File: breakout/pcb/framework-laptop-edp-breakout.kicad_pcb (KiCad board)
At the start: 4 copper layers, 46 x 59 mm, 7 parts, among them J1 20879-040E-01, J2 Conn_01x40, J3 Conn_01x01

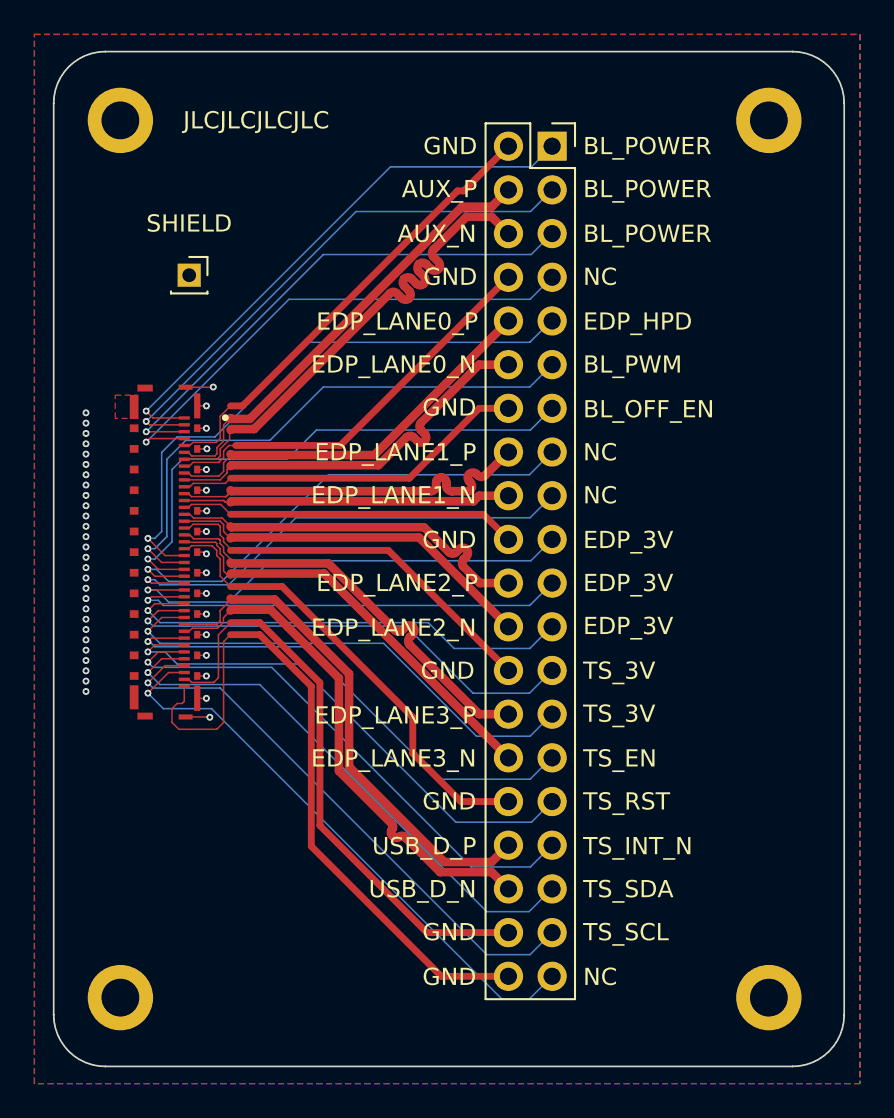
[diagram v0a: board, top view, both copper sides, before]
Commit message: rework breakout because pins were wrong
turns out pin out documentation from framework is reversed - pin 40  in pinouts.md is pin 1 on the data sheet for the ipex connector
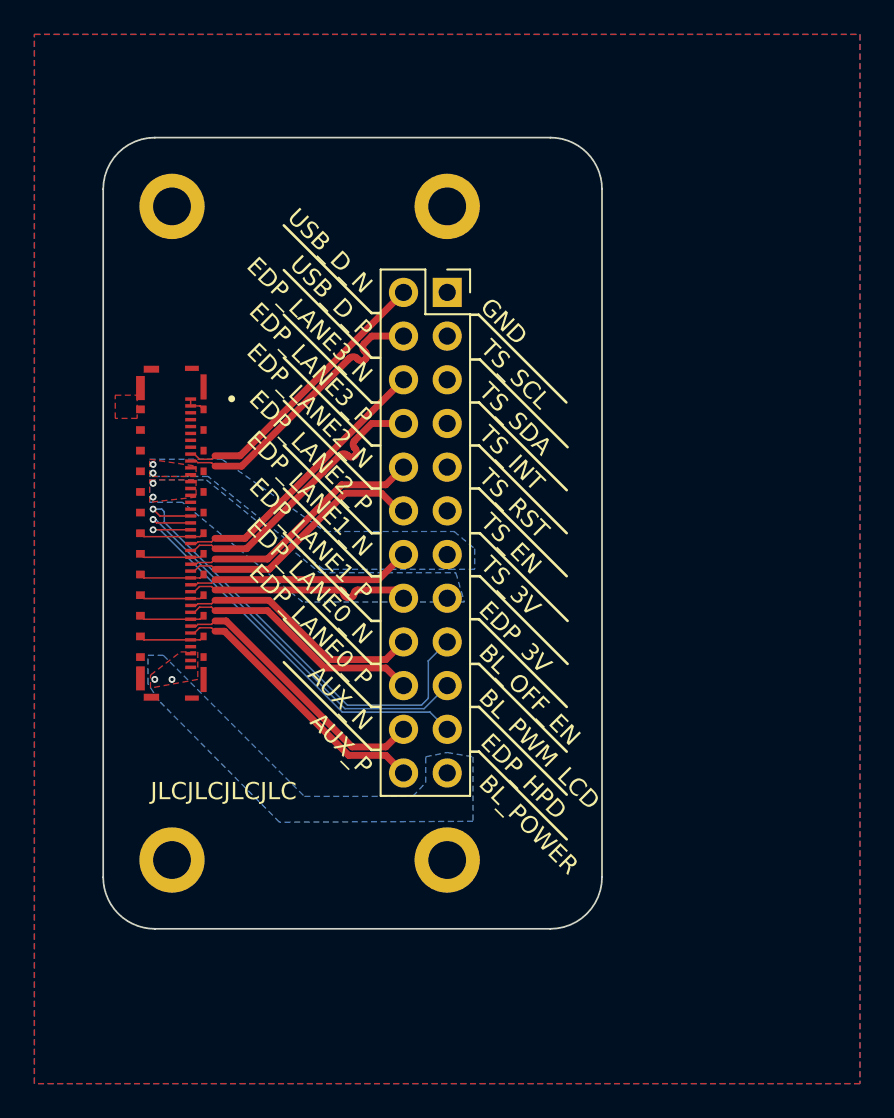
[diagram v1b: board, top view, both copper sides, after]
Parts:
- removed J3: Conn_01x01, Connector_PinSocket_2.00mm:PinSocket_1x01_P2.00mm_Vertical
- J2: footprint Connector_PinSocket_2.54mm:PinSocket_2x20_P2.54mm_Vertical -> Connector_PinSocket_2.54mm:PinSocket_2x12_P2.54mm_Vertical
- moved H4 20.3 mm to (174.0, 95.0)
- moved H3 19.4 mm to (174.0, 57.0)
- moved J2 10.5 mm to (174.0, 62.0)
- moved H2 8.54 mm to (158.0, 95.0)
- moved H1 5.83 mm to (158.0, 57.0)
- moved J1 1.16 mm to (158.0, 76.0)
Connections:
- H1 pad 1: /SHIELD -> GND
- H2 pad 1: /SHIELD -> GND
- H3 pad 1: /SHIELD -> GND
- H4 pad 1: /SHIELD -> GND
- J1 pad 1: BL_POWER_1 -> GND
- J1 pad 10: EDP_LANE0_N -> USB_D_P
- J1 pad 11: GND_3 -> TS_3V
- J1 pad 12: EDP_LANE1_P -> TS_3V
- J1 pad 13: EDP_LANE1_N -> EDP_3V
- J1 pad 14: GND_4 -> EDP_3V
- J1 pad 15: EDP_LANE2_P -> EDP_3V
- J1 pad 16: EDP_LANE2_N -> unconnected-(J1-Pad16)
- J1 pad 17: GND_5 -> unconnected-(J1-Pad17)
- J1 pad 18: EDP_LANE3_P -> BL_OFF_EN
- J1 pad 19: EDP_LANE3_N -> BL_PWM_LCD
- J1 pad 2: BL_POWER_2 -> GND
- J1 pad 20: GND_6 -> EDP_HPD
- J1 pad 21: EDP_HPD -> GND
- J1 pad 22: BL_PWM_LCD -> EDP_LANE3_N
- J1 pad 23: BL_OFF_EN -> EDP_LANE3_P
- J1 pad 24: NC_2 -> GND
- J1 pad 25: NC_3 -> EDP_LANE2_N
- J1 pad 26: EDP_3V_1 -> EDP_LANE2_P
- J1 pad 27: EDP_3V_2 -> GND
- J1 pad 28: EDP_3V_3 -> EDP_LANE1_N
- J1 pad 29: TS_3V_1 -> EDP_LANE1_P
- J1 pad 3: BL_POWER3 -> unconnected-(J1-Pad3)
- J1 pad 30: TS_3V_2 -> GND
- J1 pad 31: USB_D_P -> EDP_LANE0_N
- J1 pad 32: USB_D_N -> EDP_LANE0_P
- J1 pad 33: TS_EN -> GND
- J1 pad 34: TS_RST -> AUX_N
- J1 pad 35: TS_INT_N -> AUX_P
- J1 pad 36: TS_SDA -> GND
- J1 pad 37: TS_SCL -> unconnected-(J1-Pad37)
- J1 pad 38: NC_4 -> BL_POWER
- J1 pad 39: GND_7 -> BL_POWER
- J1 pad 4: NC_1 -> TS_SCL
- J1 pad 40: GND_8 -> BL_POWER
- J1 pad 5: GND_1 -> TS_SDA
- J1 pad 6: AUX_P -> TS_INT_N
- J1 pad 7: AUX_N -> TS_RST
- J1 pad 8: GND_2 -> TS_EN
- J1 pad 9: EDP_LANE0_P -> USB_D_N
- J1 pad S1: /SHIELD -> GND
- J1 pad S10: /SHIELD -> GND
- J1 pad S11: /SHIELD -> GND
- J1 pad S12: /SHIELD -> GND
- J1 pad S13: /SHIELD -> GND
- J1 pad S14: /SHIELD -> GND
- J1 pad S15: /SHIELD -> GND
- J1 pad S16: /SHIELD -> GND
- J1 pad S17: /SHIELD -> GND
- J1 pad S18: /SHIELD -> GND
- J1 pad S19: /SHIELD -> GND
- J1 pad S2: /SHIELD -> GND
- J1 pad S20: /SHIELD -> GND
- J1 pad S21: /SHIELD -> GND
- J1 pad S22: /SHIELD -> GND
- J1 pad S23: /SHIELD -> GND
- J1 pad S24: /SHIELD -> GND
- J1 pad S25: /SHIELD -> GND
- J1 pad S26: /SHIELD -> GND
- J1 pad S27: /SHIELD -> GND
- J1 pad S28: /SHIELD -> GND
- J1 pad S29: /SHIELD -> GND
- J1 pad S3: /SHIELD -> GND
- J1 pad S30: /SHIELD -> GND
- J1 pad S31: /SHIELD -> GND
- J1 pad S32: /SHIELD -> GND
- J1 pad S33: /SHIELD -> GND
- J1 pad S34: /SHIELD -> GND
- J1 pad S4: /SHIELD -> GND
- J1 pad S5: /SHIELD -> GND
- J1 pad S6: /SHIELD -> GND
- J1 pad S7: /SHIELD -> GND
- J1 pad S8: /SHIELD -> GND
- J1 pad S9: /SHIELD -> GND
- J2 pad 1: BL_POWER_1 -> GND
- J2 pad 10: EDP_LANE0_P -> EDP_LANE2_N
- J2 pad 11: BL_PWM_LCD -> TS_EN
- J2 pad 12: EDP_LANE0_N -> EDP_LANE2_P
- J2 pad 13: BL_OFF_EN -> TS_3V
- J2 pad 14: GND_3 -> EDP_LANE1_N
- J2 pad 15: NC_2 -> EDP_3V
- J2 pad 17: NC_3 -> BL_OFF_EN
- J2 pad 18: EDP_LANE1_N -> EDP_LANE0_N
- J2 pad 19: EDP_3V_1 -> BL_PWM_LCD
- J2 pad 2: GND_1 -> USB_D_N
- J2 pad 20: GND_4 -> EDP_LANE0_P
- J2 pad 21: EDP_3V_2 -> EDP_HPD
- J2 pad 22: EDP_LANE2_P -> AUX_N
- J2 pad 23: EDP_3V_3 -> BL_POWER
- J2 pad 24: EDP_LANE2_N -> AUX_P
- J2 pad 3: BL_POWER_2 -> TS_SCL
- J2 pad 4: AUX_P -> USB_D_P
- J2 pad 5: BL_POWER3 -> TS_SDA
- J2 pad 6: AUX_N -> EDP_LANE3_N
- J2 pad 7: NC_1 -> TS_INT_N
- J2 pad 8: GND_2 -> EDP_LANE3_P
- J2 pad 9: EDP_HPD -> TS_RST
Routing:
- net GND_8: track 41.0 -> 0.00 mm
- net GND_7: track 34.2 -> 0.00 mm
- net NC_4: track 34.0 -> 0.00 mm, vias 1 -> 0
- net TS_SCL: track 33.1 -> 0.00 mm, vias 1 -> 0
- net BL_POWER_1: track 32.4 -> 0.00 mm, vias 1 -> 0
- net TS_SDA: track 32.3 -> 0.00 mm, vias 1 -> 0
- net BL_POWER_2: track 31.5 -> 0.00 mm, vias 1 -> 0
- net TS_INT_N: track 31.3 -> 0.00 mm, vias 1 -> 0
- net BL_POWER3: track 30.6 -> 0.00 mm, vias 1 -> 0
- net TS_RST: track 30.4 -> 0.00 mm, vias 1 -> 0
- net NC_1: track 29.9 -> 0.00 mm, vias 1 -> 0
- net TS_EN: track 29.5 -> 0.00 mm, vias 1 -> 0
- net NC_2: track 29.2 -> 0.00 mm, vias 1 -> 0
- net TS_3V_2: track 29.0 -> 0.00 mm, vias 1 -> 0
- net TS_3V_1: track 28.2 -> 0.00 mm, vias 1 -> 0
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- added copper zone on B.Cu, net BL_POWER
- added copper zone on F.Cu, net BL_POWER
- added copper zone on B.Cu, net EDP_3V
- added copper zone on F.Cu, net EDP_3V
- added copper zone on B.Cu, net GND
- added copper zone on F.Cu, net GND
- added copper zone on B.Cu, net TS_3V
- added copper zone on F.Cu, net TS_3V
- removed copper zone on B.Cu, net /SHIELD
- removed copper zone on F.Cu, net /SHIELD
- removed copper zone on In1.Cu, net /SHIELD
- removed copper zone on In2.Cu, net /SHIELD
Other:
- board size 46 x 59 mm -> 29 x 46 mm
- copper layers 4 -> 2
- board text added: "BL_PWM_LCD"
- board text added: "TS_INT"
- board text removed: "BL_PWM"
- board text removed: "NC"
- board text removed: "SHIELD"
- board text removed: "TS_INT_N"

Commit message: fix breakout labels on back
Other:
- board text added: "RS_EN"
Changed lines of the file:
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@@
     )
   )
-  (gr_line (start 172.8092 63.3558) (end 172.8092 60.7142) (layer "B.SilkS") (width 0.15))
-  (gr_line (start 175.4 63.3558) (end 172.8092 63.3558) (layer "B.SilkS") (width 0.15))
-  (gr_line (start 175.3 91.2) (end 175.3 63.3558) (layer "B.SilkS") (width 0.15))
-  (gr_line (start 170.1965 91.2) (end 175.3 91.2) (layer "B.SilkS") (width 0.15))
-  (gr_line (start 170.193 60.7142) (end 170.1965 91.2) (layer "B.SilkS") (width 0.15))
-  (gr_line (start 175.3 60.7396) (end 175.3 62.0604) (layer "B.SilkS") (width 0.15))
-  (gr_line (start 173.9269 60.7396) (end 175.2731 60.7396) (layer "B.SilkS") (width 0.15))
-  (gr_line (start 172.7838 60.7142) (end 170.193 60.7142) (layer "B.SilkS") (width 0.15))
+  (gr_line (start 175.7908 63.3) (end 175.2908 63.3) (layer "B.SilkS") (width 0.15))
+  (gr_line (start 169.58 81) (end 170.079999 81) (layer "B.SilkS") (width 0.15))
+  (gr_line (start 169.53 78.5) (end 170.029999 78.5) (layer "B.SilkS") (width 0.15))
+  (gr_line (start 164.48 76) (end 169.58 70.9) (layer "B.SilkS") (width 0.15))
+  (gr_line (start 169.58 68.4) (end 170.079999 68.4) (layer "B.SilkS") (width 0.15))
+  (gr_line (start 172.7 63.3) (end 172.7 60.6584) (layer "B.SilkS") (width 0.15))
+  (gr_line (start 164.48 78.5) (end 169.58 73.4) (layer "B.SilkS") (width 0.15))
+  (gr_line (start 164.48 91.2) (end 169.58 86.1) (layer "B.SilkS") (width 0.15))
+  (gr_line (start 164.48 86.1) (end 169.58 81) (layer "B.SilkS") (width 0.15))
+  (gr_line (start 169.58 73.4) (end 170.079999 73.4) (layer "B.SilkS") (width 0.15))
+  (gr_line (start 169.53 76) (end 170.029999 76) (layer "B.SilkS") (width 0.15))
+  (gr_line (start 169.58 70.9) (end 170.079999 70.9) (layer "B.SilkS") (width 0.15))
+  (gr_line (start 175.7908 76.1) (end 175.2908 76.1) (layer "B.SilkS") (width 0.15))
+  (gr_line (start 180.8908 76.1) (end 175.7908 81.2) (layer "B.SilkS") (width 0.15))
+  (gr_line (start 180.8908 60.8) (end 175.7908 65.9) (layer "B.SilkS") (width 0.15))
+  (gr_line (start 180.8908 71) (end 175.7908 76.1) (layer "B.SilkS") (width 0.15))
+  (gr_line (start 164.48 88.7) (end 169.58 83.6) (layer "B.SilkS") (width 0.15))
+  (gr_line (start 175.2908 63.3) (end 172.7 63.3) (layer "B.SilkS") (width 0.15))
+  (gr_line (start 164.430001 71) (end 169.530001 65.9) (layer "B.SilkS") (width 0.15))
+  (gr_line (start 164.48 93.8) (end 169.58 88.7) (layer "B.SilkS") (width 0.15))
+  (gr_line (start 175.7908 73.5) (end 175.2908 73.5) (layer "B.SilkS") (width 0.15))
+  (gr_line (start 175.3 91.3) (end 175.2908 63.3) (layer "B.SilkS") (width 0.15))
+  (gr_line (start 180.8908 65.9) (end 175.7908 71) (layer "B.SilkS") (width 0.15))
+  (gr_line (start 170.1092 91.3) (end 175.3 91.3) (layer "B.SilkS") (width 0.15))
+  (gr_line (start 175.7908 71) (end 175.2908 71) (layer "B.SilkS") (width 0.15))
+  (gr_line (start 170.1092 60.6584) (end 170.1092 91.3) (layer "B.SilkS") (width 0.15))
+  (gr_line (start 180.8908 83.6) (end 175.7908 88.7) (layer "B.SilkS") (width 0.15))
+  (gr_line (start 175.3 60.7) (end 175.3 62.0208) (layer "B.SilkS") (width 0.15))
+  (gr_line (start 175.7908 83.7) (end 175.2908 83.7) (layer "B.SilkS") (width 0.15))
+  (gr_line (start 173.9269 60.7) (end 175.2731 60.7) (layer "B.SilkS") (width 0.15))
+  (gr_line (start 180.8908 73.5) (end 175.7908 78.6) (layer "B.SilkS") (width 0.15))
+  (gr_line (start 169.58 88.7) (end 170.079999 88.7) (layer "B.SilkS") (width 0.15))
+  (gr_line (start 180.8908 63.4) (end 175.7908 68.5) (layer "B.SilkS") (width 0.15))
+  (gr_line (start 175.7908 68.5) (end 175.2908 68.5) (layer "B.SilkS") (width 0.15))
+  (gr_line (start 169.600001 63.3) (end 170.1 63.3) (layer "B.SilkS") (width 0.15))
+  (gr_line (start 175.7908 86.2) (end 175.2908 86.2) (layer "B.SilkS") (width 0.15))
+  (gr_line (start 164.500001 68.4) (end 169.600001 63.3) (layer "B.SilkS") (width 0.15))
+  (gr_line (start 175.7908 65.9) (end 175.2908 65.9) (layer "B.SilkS") (width 0.15))
+  (gr_line (start 172.7 60.6584) (end 170.1092 60.6584) (layer "B.SilkS") (width 0.15))
+  (gr_line (start 180.8908 68.4) (end 175.7908 73.5) (layer "B.SilkS") (width 0.15))
+  (gr_line (start 169.58 83.6) (end 170.079999 83.6) (layer "B.SilkS") (width 0.15))
+  (gr_line (start 169.58 86.1) (end 170.079999 86.1) (layer "B.SilkS") (width 0.15))
+  (gr_line (start 164.43 83.6) (end 169.53 78.5) (layer "B.SilkS") (width 0.15))
+  (gr_line (start 180.8908 78.6) (end 175.7908 83.7) (layer "B.SilkS") (width 0.15))
+  (gr_line (start 164.43 81.1) (end 169.53 76) (layer "B.SilkS") (width 0.15))
+  (gr_line (start 175.7908 88.7) (end 175.2908 88.7) (layer "B.SilkS") (width 0.15))
+  (gr_line (start 180.8908 81.1) (end 175.7908 86.2) (layer "B.SilkS") (width 0.15))
+  (gr_line (start 175.7908 78.6) (end 175.2908 78.6) (layer "B.SilkS") (width 0.15))
+  (gr_line (start 164.48 73.5) (end 169.58 68.4) (layer "B.SilkS") (width 0.15))
+  (gr_line (start 175.7908 81.2) (end 175.2908 81.2) (layer "B.SilkS") (width 0.15))
+  (gr_line (start 180.8908 58.2) (end 175.7908 63.3) (layer "B.SilkS") (width 0.15))
+  (gr_line (start 169.530001 65.9) (end 170.03 65.9) (layer "B.SilkS") (width 0.15))
   (gr_line (start 170.1 88.6) (end 169.6 88.6) (layer "F.SilkS") (width 0.15))
   (gr_line (start 169.6 83.6) (end 164.5 78.5) (layer "F.SilkS") (width 0.15))
@@
   (gr_arc (start 153.99998 56) (mid 154.878661 53.878687) (end 156.99998 53) (layer "Edge.Cuts") (width 0.1))
   (gr_line (start 183 56) (end 183 96) (layer "Edge.Cuts") (width 0.1))
+  (gr_text "EDP_LANE1_P" (at 169.33 80.2 45) (layer "B.SilkS")
+    (effects (font (size 1 1) (thickness 0.125)) (justify left mirror))
+  )
+  (gr_text "TS_SCL" (at 175.9908 64.5 45) (layer "B.SilkS")
+    (effects (font (size 1 1) (thickness 0.125)) (justify right mirror))
+  )
+  (gr_text "TS_SDA" (at 175.9908 67.1 45) (layer "B.SilkS")
+    (effects (font (size 1 1) (thickness 0.125)) (justify right mirror))
+  )
+  (gr_text "TS_3V" (at 175.9908 77.2 45) (layer "B.SilkS")
+    (effects (font (size 1 1) (thickness 0.125)) (justify right mirror))
+  )
+  (gr_text "TS_INT" (at 175.9908 69.6 45) (layer "B.SilkS")
+    (effects (font (size 1 1) (thickness 0.125)) (justify right mirror))
+  )
+  (gr_text "EDP_LANE3_N" (at 169.33 67.5 45) (layer "B.SilkS")
+    (effects (font (size 1 1) (thickness 0.125)) (justify left mirror))
+  )
+  (gr_text "EDP_3V" (at 175.9908 79.8 45) (layer "B.SilkS")
+    (effects (font (size 1 1) (thickness 0.125)) (justify right mirror))
+  )
+  (gr_text "TS_RST" (at 175.9908 72.1 45) (layer "B.SilkS")
+    (effects (font (size 1 1) (thickness 0.125)) (justify right mirror))
+  )
+  (gr_text "EDP_LANE0_N" (at 169.33 82.7 45) (layer "B.SilkS")
+    (effects (font (size 1 1) (thickness 0.125)) (justify left mirror))
+  )
+  (gr_text "EDP_LANE2_P" (at 169.23 75.1 45) (layer "B.SilkS")
+    (effects (font (size 1 1) (thickness 0.125)) (justify left mirror))
+  )
+  (gr_text "AUX_N" (at 169.23 87.9 45) (layer "B.SilkS")
+    (effects (font (size 1 1) (thickness 0.125)) (justify left mirror))
+  )
+  (gr_text "USB_D_P" (at 169.23 65 -315) (layer "B.SilkS")
+    (effects (font (size 1 1) (thickness 0.125)) (justify left mirror))
+  )
+  (gr_text "AUX_P" (at 169.33 90.3 45) (layer "B.SilkS")
+    (effects (font (size 1 1) (thickness 0.125)) (justify left mirror))
+  )
+  (gr_text "RS_EN" (at 175.9908 74.7 45) (layer "B.SilkS")
+    (effects (font (size 1 1) (thickness 0.125)) (justify right mirror))
+  )
+  (gr_text "GND" (at 175.9908 61.9 45) (layer "B.SilkS")
+    (effects (font (size 1 1) (thickness 0.125)) (justify right mirror))
+  )
   (gr_text "Framework Laptop\nI-PEX 20879-040E Breakout\nfor eDP / Touchscreen\n" (at 157.5 75.2 90) (layer "B.SilkS")
     (effects (font (size 1 1) (thickness 0.15)) (justify mirror))
   )
+  (gr_text "BL_OFF_EN" (at 175.9908 82.3 45) (layer "B.SilkS")
+    (effects (font (size 1 1) (thickness 0.125)) (justify right mirror))
+  )
+  (gr_text "EDP_HPD" (at 175.9908 87.3 45) (layer "B.SilkS")
+    (effects (font (size 1 1) (thickness 0.125)) (justify right mirror))
+  )
+  (gr_text "BL_PWM_LCD" (at 175.9908 84.8 45) (layer "B.SilkS")
+    (effects (font (size 1 1) (thickness 0.125)) (justify right mirror))
+  )
+  (gr_text "BL_POWER" (at 175.9908 89.9 45) (layer "B.SilkS")
+    (effects (font (size 1 1) (thickness 0.125)) (justify right mirror))
+  )
+  (gr_text "EDP_LANE0_P" (at 169.33 85.3 45) (layer "B.SilkS")
+    (effects (font (size 1 1) (thickness 0.125)) (justify left mirror))
+  )
+  (gr_text "USB_D_N" (at 168.567734 62.8 45) (layer "B.SilkS")
+    (effects (font (size 1 1) (thickness 0.125)) (justify left mirror))
+  )
+  (gr_text "EDP_LANE1_N" (at 169.23 77.6 45) (layer "B.SilkS")
+    (effects (font (size 1 1) (thickness 0.125)) (justify left mirror))
+  )
+  (gr_text "EDP_LANE2_N" (at 169.33 72.5 45) (layer "B.SilkS")
+    (effects (font (size 1 1) (thickness 0.125)) (justify left mirror))
+  )
+  (gr_text "EDP_LANE3_P" (at 169.33 70 45) (layer "B.SilkS")
+    (effects (font (size 1 1) (thickness 0.125)) (justify left mirror))
+  )
   (gr_text "AUX_N" (at 169.4 87.2 -45) (layer "F.SilkS")
